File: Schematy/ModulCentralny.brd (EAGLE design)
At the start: 109.2 x 50.6 mm, 47 parts, among them X1 GLX-S-88M

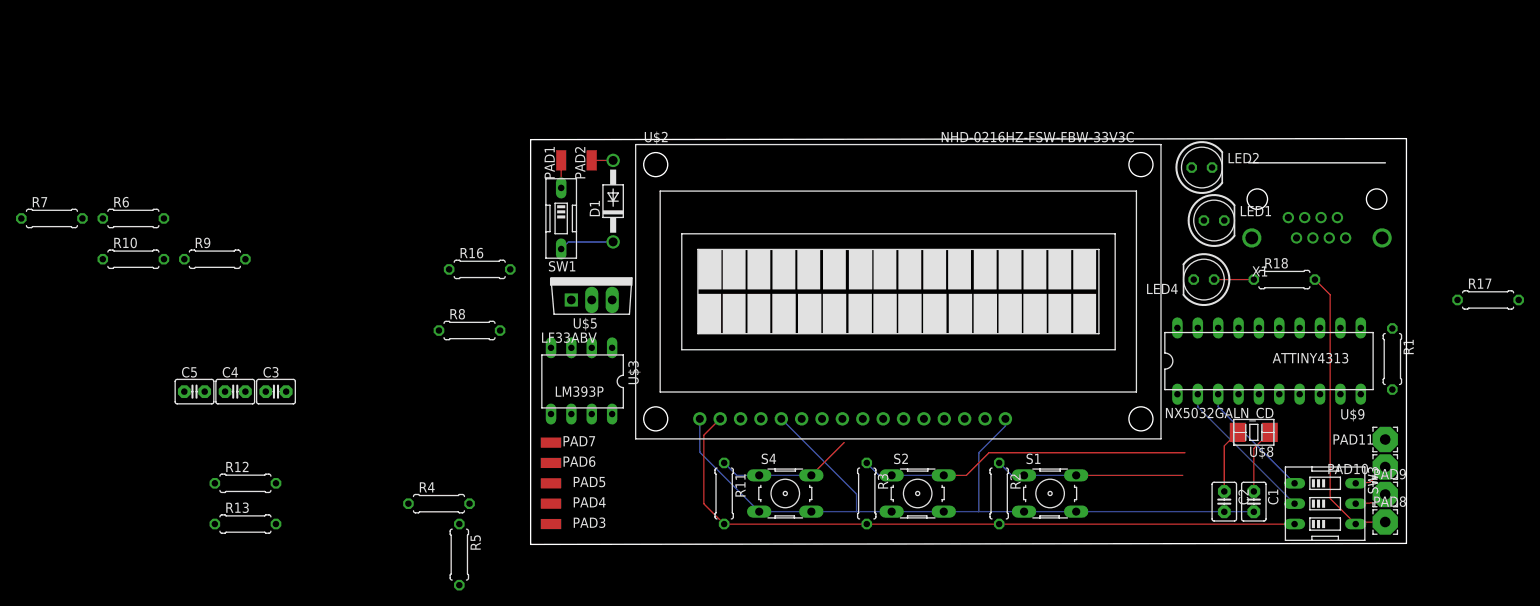
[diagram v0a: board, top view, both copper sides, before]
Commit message: Dodanie podciągającego rezystora na wyjście lm393
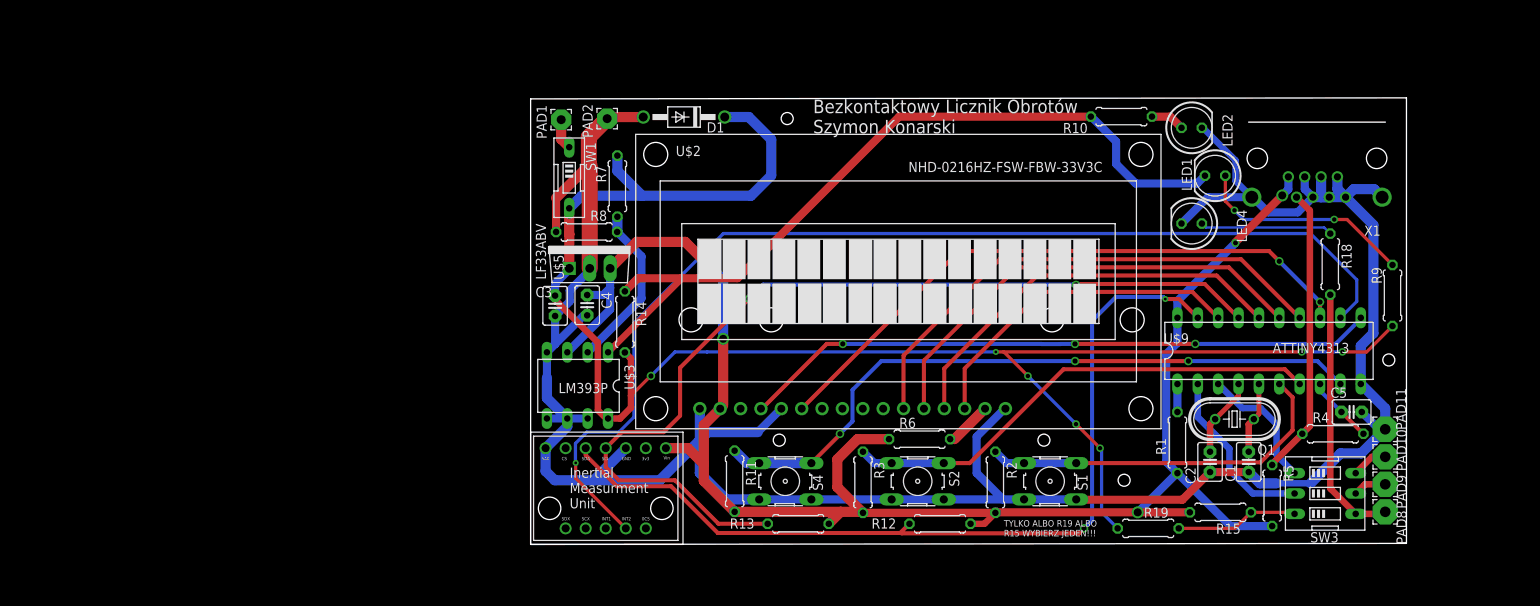
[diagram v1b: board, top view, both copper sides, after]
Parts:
- removed PAD3: BMI160 SDA, wirepad:SMD1,27-2,54
- removed PAD4: BMI160 SCL, wirepad:SMD1,27-2,54
- removed PAD5: BMI160 VCC, wirepad:SMD1,27-2,54
- removed PAD6: BMI160 GND, wirepad:SMD1,27-2,54
- removed PAD7: BMI160 SA0, wirepad:SMD1,27-2,54
- removed R16, R17: 15k, rcl:0207/7
- removed U$8: NX5032GALN_CD, BezkonataktowyLicznikObrotów:NX5032GA
- added Q1: 10MHz, crystal:HC49U70
- added R14, R15, R19: 5k, rcl:0207/7
- added U$1: BMI160PODOBNY, BezkonataktowyLicznikObrotów:BMI160MODULE
- PAD1, PAD2: device wirepad:SMD1,27-2,54 -> wirepad:2,54/1,1
- R10, R18, R9: value 5k -> 10k
- R6: value 5k -> 4.7k
- SW1: value (none) -> Włącznik
- SW3: value (none) -> Opcje UART
- moved R9 146.9 mm to (107.5, 31.0), turned to 270 degrees
- moved C5 144.3 mm to (102.4, 16.5)
- moved R10 124.5 mm to (73.7, 53.3), turned to 180 degrees
- moved R4 111.8 mm to (100.0, 13.8)
- moved R6 101.8 mm to (48.5, 13.1)
- moved R5 101.6 mm to (92.5, 6.10)
- moved R12 86.7 mm to (51.0, 2.57)
- moved R7 70.6 mm to (10.8, 44.7), turned to 90 degrees
- moved R13 68.9 mm to (33.4, 2.57)
- moved C4 45.2 mm to (7.05, 29.8), turned to 270 degrees
- moved C3 36.4 mm to (3.05, 29.8), turned to 270 degrees
- moved R1 28.7 mm to (80.6, 12.7), turned to 90 degrees
- moved R8 19.1 mm to (6.98, 39.0)
- moved D1 13.7 mm to (19.1, 53.3), turned to 180 degrees
- moved LED4 7.15 mm to (82.4, 40.0)
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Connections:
- removed net N$33: R16.2, R17.1, U$9.12
- new net N$14: R15.1, R19.1, SW3.3
- new net N$24: U$1.INT2, U$9.12
- net GND: now also U$1.GND, U$1.SA0; no longer PAD6.1, PAD7.1, R16.1
- net N$1: now also U$1.SCL; no longer PAD4.1
- net N$15: now also Q1.1; no longer U$8.1
- net N$16: now also R6.2; no longer R6.1
- net N$17: now also R14.2, R19.2; no longer R17.2
- net N$18: now also U$1.SDA; no longer PAD3.1
- net N$2: now also Q1.2; no longer U$8.2
- net N$20: now also R14.1
- net VCC: now also R15.2, R6.1, U$1.VIN; no longer PAD5.1, R6.2, SW3.3
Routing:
- net GND: track 107.4 -> 314.5 mm
- net N$17: track 6.85 -> 211.7 mm, vias 0 -> 7
- net N$24: track 0.00 -> 136.3 mm, vias 0 -> 1
- net VCC: track 86.1 -> 216.9 mm, vias 0 -> 5
- net N$1: track 0.00 -> 118.1 mm, vias 0 -> 2
- net N$18: track 0.00 -> 110.7 mm, vias 0 -> 2
- net N$20: track 0.00 -> 100.1 mm
- net N$23: track 0.00 -> 79.6 mm, vias 0 -> 3
- net N$9: track 0.00 -> 77.4 mm, vias 0 -> 2
- net N$4: track 17.3 -> 85.0 mm, vias 0 -> 3
- net N$8: track 0.00 -> 64.0 mm
- net N$7: track 0.00 -> 57.7 mm
- net N$6: track 0.00 -> 51.2 mm
- net N$5: track 0.00 -> 41.9 mm
- net N$10: track 0.00 -> 36.0 mm
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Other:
- board size 109.2 x 50.6 mm -> 109.2 x 55.7 mm
- board text added: "Bezkontaktowy Licznik Obrotów Szymon Konarski"
- board text added: "TYLKO ALBO R19 ALBO R15 WYBIERZ JEDEN!!!"

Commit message: Nowa płytka w wymiarach 6,6x9,9mm
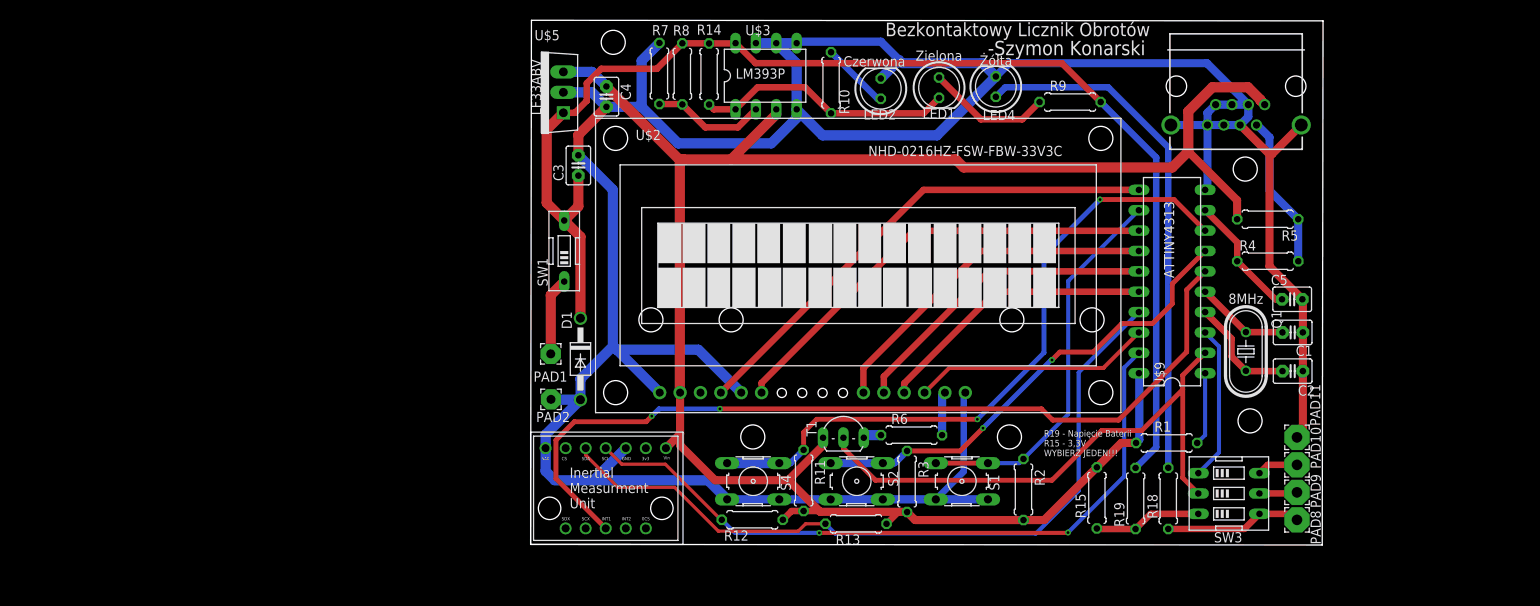
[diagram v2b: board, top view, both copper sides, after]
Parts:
- added T1: (no value), transistor:TO92-CBE
- C5: value 1n -> 0.1u
- Q1: value 10MHz -> 8MHz
- R4: value 100 -> 15k
- R5: value 2k -> 5k
- R6: value 4.7k -> 5k
- moved R9 46.9 mm to (67.3, 55.2), turned to 0 degrees
- moved U$3 45.3 mm to (29.4, 58.4), turned to 0 degrees
- moved LED2 39.1 mm to (43.7, 56.8), turned to 90 degrees
- moved R10 36.4 mm to (37.5, 57.6), turned to 270 degrees
- moved LED1 36.1 mm to (50.9, 56.9), turned to 270 degrees
- moved PAD2 35.7 mm to (2.54, 18.1)
- moved R18 35.5 mm to (79.5, 5.74)
- moved R5 34.5 mm to (91.9, 40.5), turned to 180 degrees
- moved D1 32.8 mm to (6.21, 23.1), turned to 270 degrees
- moved R14 32.6 mm to (22.3, 58.7), turned to 90 degrees
- moved LED4 29.8 mm to (58.0, 57.1), turned to 90 degrees
- moved PAD1 29.2 mm to (2.51, 23.8)
- moved C4 26.1 mm to (9.45, 55.8)
- moved R12 23.4 mm to (27.6, 3.07)
- moved R4 23.0 mm to (91.9, 35.3), turned to 180 degrees
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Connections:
- new net N$25: R6.1, T1.E
- net N$1: now also U$1.SDA; no longer U$1.SCL
- net N$13: now also T1.B
- net N$18: now also U$1.SCL; no longer U$1.SDA
- net N$24: now also U$1.INT1, U$9.6; no longer U$1.INT2, U$9.12
- net N$30: now also U$9.9; no longer U$9.8
- net N$32: now also U$9.12; no longer U$9.6
- net N$4: now also U$9.8; no longer U$9.9
- net VCC: now also T1.C; no longer R6.1
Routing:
- net GND: track 314.5 -> 384.6 mm
- net N$20: track 100.1 -> 32.2 mm
- net N$17: track 211.7 -> 159.0 mm, vias 7 -> 0
- net N$37: track 16.5 -> 65.0 mm
- net N$13: track 21.7 -> 69.4 mm
- net VCC: track 216.9 -> 247.2 mm, vias 5 -> 0
- net N$24: track 136.3 -> 108.9 mm, vias 1 -> 2
- net N$1: track 118.1 -> 94.7 mm, vias 2 -> 0
- net N$18: track 110.7 -> 88.1 mm
- net N$9: track 77.4 -> 56.1 mm, vias 2 -> 0
- net N$8: track 64.0 -> 43.5 mm
- net N$7: track 57.7 -> 39.2 mm
- net N$23: track 79.6 -> 62.6 mm, vias 3 -> 0
- net N$10: track 36.0 -> 19.2 mm
- net N$6: track 51.2 -> 35.1 mm
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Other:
- board size 109.2 x 55.7 mm -> 98.8 x 65.4 mm
- board text added: "-Szymon Konarski"
- board text added: "8MHz"
- board text added: "Bezkontaktowy Licznik Obrotów"
- board text added: "Czerwona"
- board text added: "Projekt bezkontaktowego dwumodułowego obrotomierza wykonany na zajęcia z przedmiotu "Systemy Mikroprocesorowe i Wbudowane", Politechnika Śląska, kierunek - Informatyka. Szymon Konarski - 2025/26"
- board text added: "R19 - Napięcie Baterii R15 - 3,3V WYBIERZ JEDEN!!!"
- board text added: "Zielona"
- board text added: "Żółta"
- board text removed: "Bezkontaktowy Licznik Obrotów Szymon Konarski"
- board text removed: "TYLKO ALBO R19 ALBO R15 WYBIERZ JEDEN!!!"
